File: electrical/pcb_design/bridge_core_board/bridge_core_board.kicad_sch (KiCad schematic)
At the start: 1 part

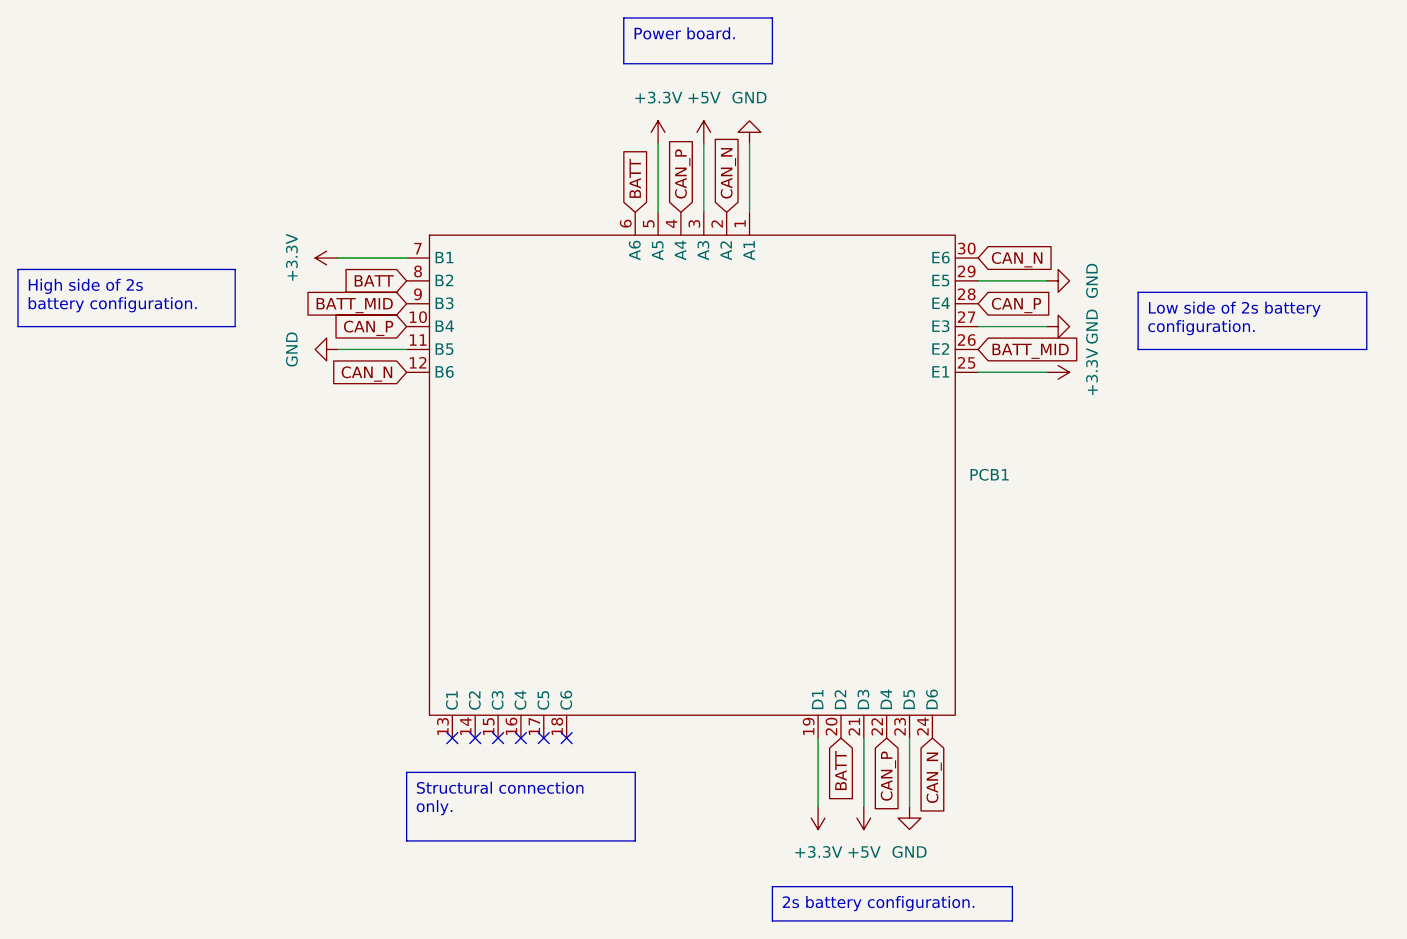
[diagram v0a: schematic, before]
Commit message: Updated bridge core board with new backplane pinout
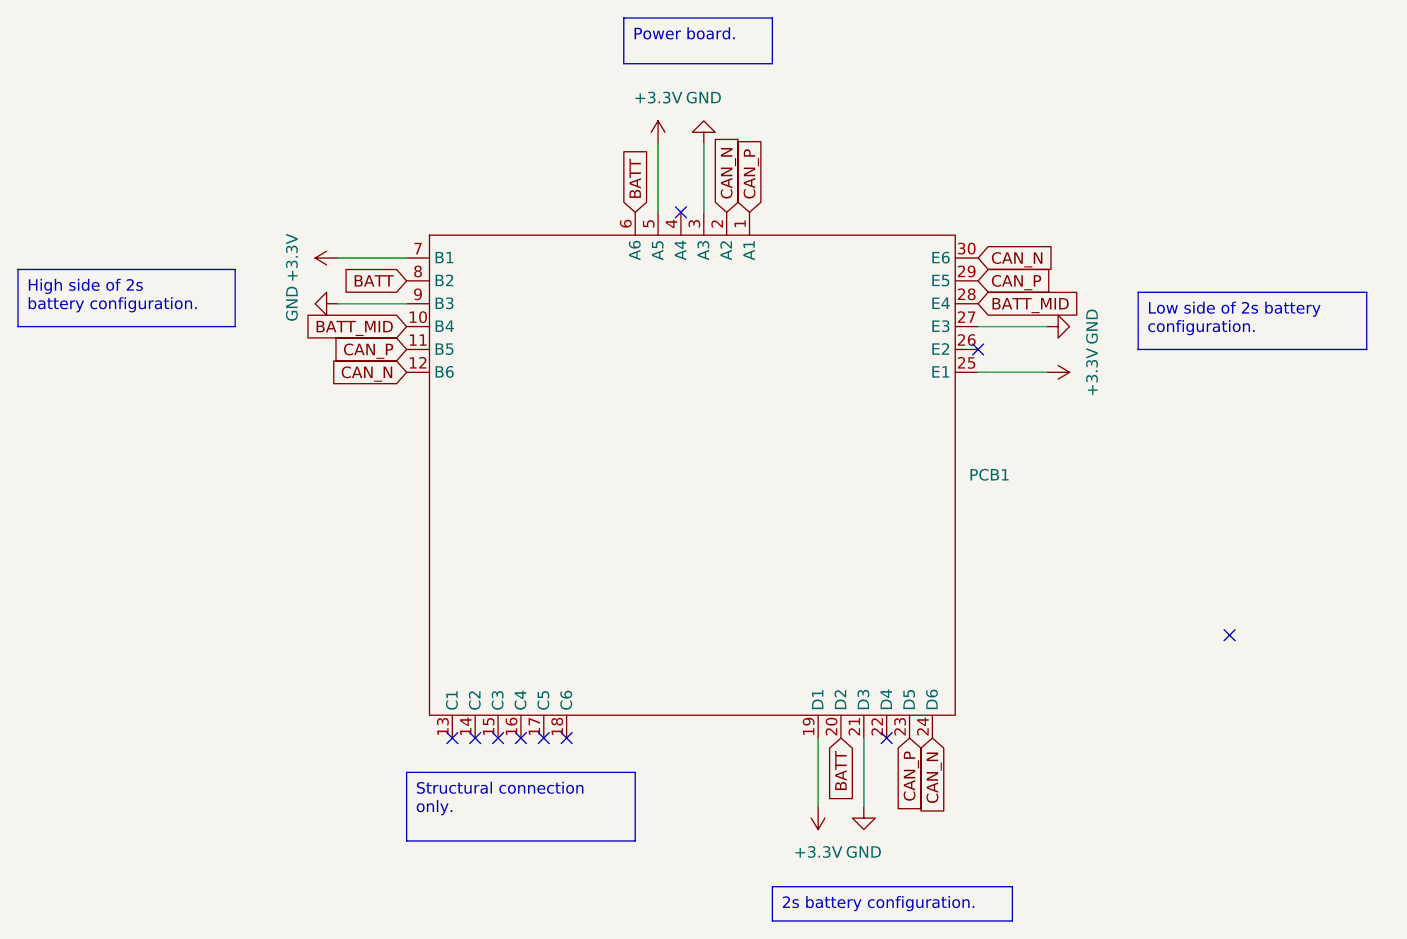
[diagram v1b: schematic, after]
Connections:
- net +5V is gone; now on net GND: PCB1.21 (D3), PCB1.3 (A3)
- net BATT_MID: now also PCB1.10 (B4), PCB1.28 (E4); no longer PCB1.26 (E2), PCB1.9 (B3)
- net CAN_P: now also PCB1.1 (A1), PCB1.11 (B5), PCB1.23 (D5), PCB1.29 (E5); no longer PCB1.10 (B4), PCB1.22 (D4), PCB1.28 (E4), PCB1.4 (A4)
- net GND: now also PCB1.9 (B3); no longer PCB1.1 (A1), PCB1.11 (B5), PCB1.23 (D5), PCB1.29 (E5)
- no-connect marks 6 -> 10
